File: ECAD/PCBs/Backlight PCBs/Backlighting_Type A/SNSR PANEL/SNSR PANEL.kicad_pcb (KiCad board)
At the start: 2 copper layers, 137.2 x 76.2 mm, 127 parts, among them J1 Conn_01x04_Female, J2 Conn_01x04_Female

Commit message: Drawing Sheet & Silkscreen update - Backlight Panels (Fc thru Spin)
1:  Updated/Relinked Drawing Sheet for both PCB and Schematics
2:  Standardized Silkscreen (if required)

Finished Remaining Backlighting Type A & Type B PCBs.....
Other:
- board text added: "SNSR PANEL Revision: 3 www.openhornet.com"
- board text removed: "SNSR Panel Backlight Designed by L. Walker"
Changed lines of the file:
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@@
   )
   (paper "A4")
+  (title_block
+    (title "SNSR PANEL")
+    (date "2023-02-10")
+    (rev "3")
+  )
   (layers
     (0 "F.Cu" signal)
@@
     (effects (font (size 1 1) (thickness 0.15)) (justify mirror))
   )
-  (gr_text "SNSR Panel Backlight\nDesigned by L. Walker" (at 121.2 83.4) (layer "B.SilkS")
-    (effects (font (size 1 1) (thickness 0.15)) (justify left mirror))
+  (gr_text "SNSR PANEL\nRevision: 3\nwww.openhornet.com" (at 156.4132 88.0618) (layer "B.SilkS")
+    (effects (font (size 1 1) (thickness 0.15)) (justify mirror))
   )
   (gr_text "POWER REQUIREMENTS:\nVOLTAGE: 5V DC\nLEDS: 58\nCURRENT: 3.48A\nWATTAGE: 17.4W" (at 199.7456 88.8746) (layer "B.SilkS")

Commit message: Review: SIM CTRL thru SPIN RCV 100% - minus SEL JETT
Reviewed/adjusted silkscreens as needed
Relinked footprints
Updated Manufacturing files
Updated PNGs and STEP files as needed.
Renamed PNGs for standardization
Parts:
- 1, 2: footprint OH_Backlighting:OH_Panel_6-32_PHS -> OH_Footprints:OH_Panel_6-32_PHS
- 3, 5: footprint OH_Backlighting:100SPX_Toggle_13mm_x_18mm -> OH_Footprints:100SPX_Toggle_13mm_x_18mm
- 4: footprint OH_Backlighting:631H_Toggle_13mm_x_13mm -> OH_Footprints:631H_Toggle_13mm_x_13mm
- G***: footprint OH_Backlighting:100SP3_Toggle_Silkscreen -> OH_Footprints:100SP3_Toggle_Silkscreen
- G***: footprint OH_Backlighting:631H_Toggle_Silkscreen -> OH_Footprints:631H_Toggle_Silkscreen
- G***: footprint OH_Backlighting:100SP1_Toggle_Silkscreen -> OH_Footprints:100SP1_Toggle_Silkscreen
- G***: footprint OH_General:CC-BY-NC-SA-Small -> OH_Footprints:CC-BY-NC-SA-Small
- G***: footprint OH_General:OH_LOGO_37.7mm_5.9mm -> OH_Footprints:OH_LOGO_37.7mm_5.9mm
- G*** (x2): footprint OH_Backlighting:A12505RNZQ - SWITCH, ROTARY, 45 DEG -> OH_Footprints:A12505RNZQ - SWITCH, ROTARY, 45 DEG

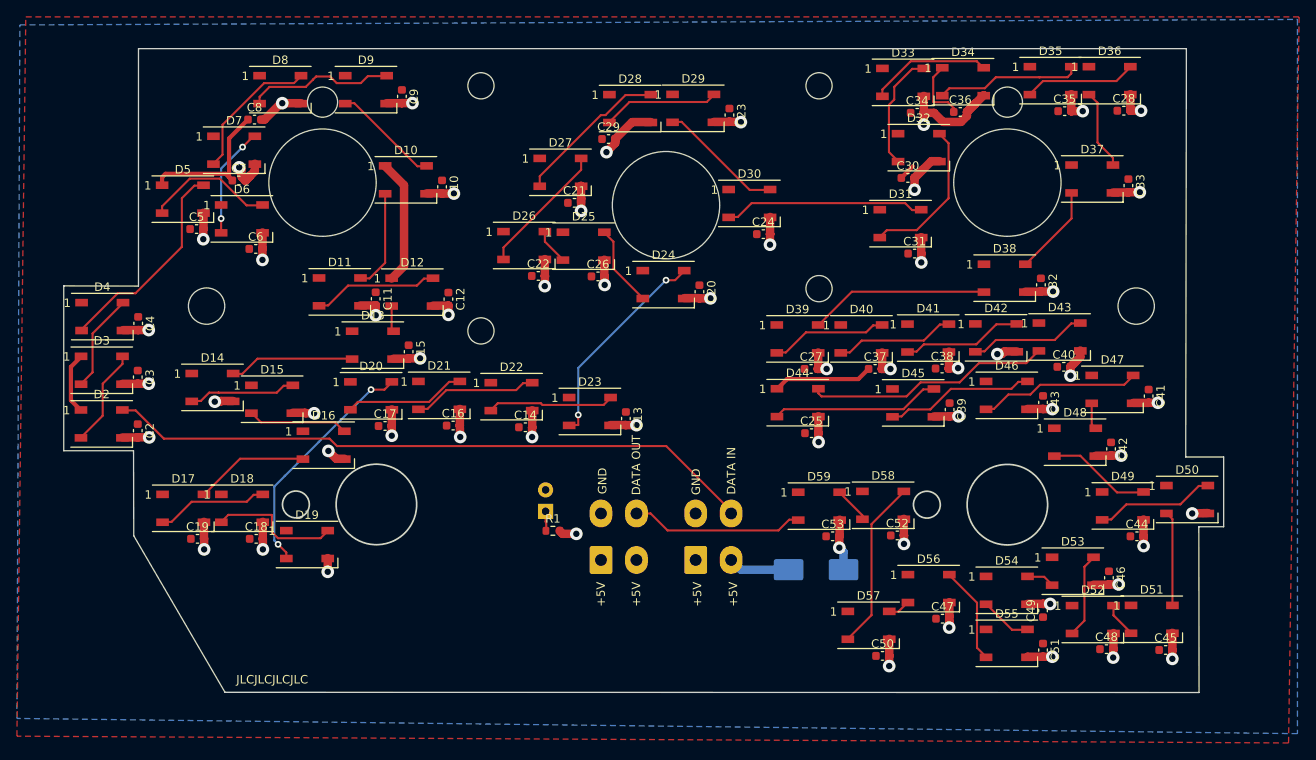
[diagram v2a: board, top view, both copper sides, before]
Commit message: KiCad 7 Transition - SNSR Panel
PCB and Schematic standardization
Updated silkscreen text
Adjusted traces to prevent conflicts
Add Testpoints
Recompiled assets and manufacturing files
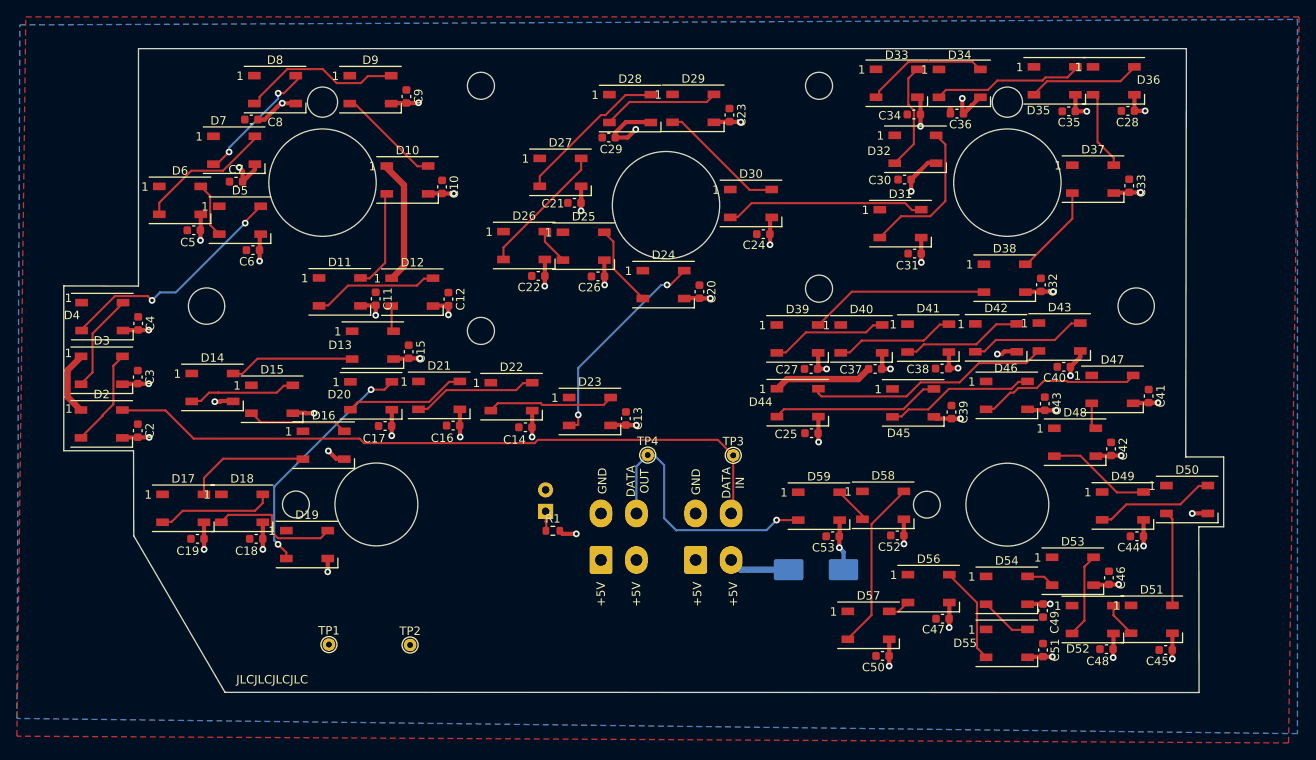
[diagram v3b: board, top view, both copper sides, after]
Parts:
- added MH10: Switch_Rotary_8pos45Deg, OH_Footprints:A12505RNZQ - SWITCH, ROTARY, 45 DEG, 8-POS, F.Cu at (117.6, 103.5)
- added MH11: Switch_Rotary_8pos45Deg, OH_Footprints:A12505RNZQ - SWITCH, ROTARY, 45 DEG, 8-POS, F.Cu at (192.3, 103.6)
- added MH3: M3 / 3.2mm, OH_Footprints:MountingHole_3.2mm_M3_DIN965, B.Cu at (130.0, 54.0)
- added MH4: M3 / 3.2mm, OH_Footprints:MountingHole_3.2mm_M3_DIN965, B.Cu at (170.0, 54.0)
- added MH5: M3 / 3.2mm, OH_Footprints:MountingHole_3.2mm_M3_DIN965, B.Cu at (130.0, 83.0)
- added MH6: M3 / 3.2mm, OH_Footprints:MountingHole_3.2mm_M3_DIN965, B.Cu at (170.0, 78.0)
- added TP1: TestPoint, OH_Footprints:TestPoint_THTPad_D1.5mm_Drill0.7mm, F.Cu at (112.0, 120.1)
- added TP2: TestPoint, OH_Footprints:TestPoint_THTPad_D1.5mm_Drill0.7mm, F.Cu at (121.6, 120.2)
- added TP3: TestPoint, OH_Footprints:TestPoint_THTPad_D1.5mm_Drill0.7mm, F.Cu at (159.8, 97.7)
- added TP4: TestPoint, OH_Footprints:TestPoint_THTPad_D1.5mm_Drill0.7mm, F.Cu at (149.7, 97.7)
- C1: value C_Polarized -> 1000uF
- C10, C11, C12, C13, C14, C15, C16, C17, C18, C19, C2, C20, C21, C22, C23, C24, C25, C26, C27, C28, C29, C3, C30, C31, C32, C33, C34, C35, C36, C37, C38, C39, C4, C40, C41, C42, C43, C44, C45, C46, C47, C48, C49, C5, C50, C51, C52, C53, C6, C7, C8, C9: value C -> 0.1uF
- D1: value LED -> Green
- J1, J2: value Conn_01x04_Female -> Mini-Fit Jr. 2x02
- LOGO1: renamed from G***; footprint OH_Footprints:OH_LOGO_37.7mm_5.9mm -> OH_Footprints:LOGO_OH_Text_Small
- LOGO2: renamed from G***; footprint OH_Footprints:CC-BY-NC-SA-Small -> OH_Footprints:LOGO_CC-BY-NC-SA_Half_Small
- LOGO3: renamed from G***; value 100SP3 Toggle -> LOGO; moved to B.Cu
- LOGO4: renamed from G***; value 631H Toggle -> LOGO; footprint OH_Footprints:631H_Toggle_Silkscreen -> OH_Footprints:631H2_Toggle_Silkscreen; moved to B.Cu
- LOGO5: renamed from G***; value 100SP1 Toggle -> LOGO; moved to B.Cu
- MH1: renamed from 2; value OH_Panel_Fastner_Keepout -> 6x32 / 4mm; footprint OH_Footprints:OH_Panel_6-32_PHS -> OH_Footprints:MountingHole_6-32_PHS; moved to B.Cu
- MH2: renamed from 1; value OH_Panel_Fastner_Keepout -> 6x32 / 4mm; footprint OH_Footprints:OH_Panel_6-32_PHS -> OH_Footprints:MountingHole_6-32_PHS; moved to B.Cu
- MH7: renamed from 3; value 100SPX_Toggle_13mm_x_18mm -> Switch_100SPx
- MH8: renamed from 5; value 100SPX_Toggle_13mm_x_18mm -> Switch_100SPx
- MH9: renamed from 4; value 631H_Toggle_13mm_x_13mm -> Switch_631H; footprint OH_Footprints:631H_Toggle_13mm_x_13mm -> OH_Footprints:631HX_Toggle_13mm_x_13mm
- R1: value R -> 470
- moved LOGO2 83.5 mm to (160.5, 50.1)
- moved LOGO1 2.08 mm to (153.6, 122.2)
- moved LOGO5 1.36 mm to (202.7, 64.9), turned to 180 degrees
- moved LOGO4 0.77 mm to (163.4, 67.0), turned to 180 degrees
- moved D33 0.76 mm to (179.2, 53.7)
- moved LOGO3 0.70 mm to (121.8, 65.0), turned to 180 degrees
- moved D8 0.62 mm to (105.6, 54.5)
- moved C9 0.53 mm to (121.2, 55.3)
- moved D9 0.53 mm to (116.9, 54.5)
- moved D35 0.48 mm to (197.9, 53.4)
- moved D36 0.48 mm to (204.9, 53.4)
- moved C28 0.48 mm to (206.5, 57.0)
- moved C35 0.48 mm to (199.5, 57.0)
- moved C34 0.44 mm to (181.2, 57.4)
- moved D32 0.44 mm to (181.4, 61.5)
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- renumbered D6 to D5, D5 to D6, G*** to LOGO6, G*** to LOGO7
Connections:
- net /DATAIN renamed DATA IN
- net /DATAOUT renamed DATA OUT
- net /LED+5V renamed +5V
- net /LEDGND renamed GND
- net Net-(D16-Pad2) renamed /DATA1
- net Net-(D31-Pad2) renamed /DATA2
- net Net-(D45-Pad2) renamed /DATA3
- D4 pad 2: Net-(D4-Pad2) -> Net-(D4-DOUT)
- D5 pad 2: Net-(D6-Pad2) -> Net-(D5-DOUT)
- D5 pad 4: Net-(D5-Pad2) -> Net-(D4-DOUT)
- D6 pad 2: Net-(D5-Pad2) -> Net-(D6-DOUT)
- D6 pad 4: Net-(D4-Pad2) -> Net-(D5-DOUT)
- D7 pad 4: Net-(D6-Pad2) -> Net-(D6-DOUT)
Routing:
- net Net-(D4-DOUT): track 0.00 -> 27.7 mm, vias 0 -> 2
- net +5V: track 68.9 -> 42.0 mm
- net Net-(D4-Pad2): track 24.9 -> 0.00 mm
- net Net-(D6-DOUT): track 0.00 -> 15.8 mm
- net Net-(D5-Pad2): track 15.3 -> 0.00 mm
- net Net-(D6-Pad2): track 13.1 -> 0.00 mm, vias 2 -> 0
- net DATA OUT: track 20.5 -> 33.1 mm, vias 0 -> 1
- net Net-(D5-DOUT): track 0.00 -> 6.56 mm
- net GND: track 202.6 -> 196.8 mm, vias 58 -> 59
- net DATA IN: track 77.2 -> 81.4 mm
- net Net-(D7-DOUT): track 16.7 -> 14.9 mm, vias 0 -> 2
- net /DATA1: track 13.5 -> 14.6 mm
- net Net-(D32-DOUT): track 13.9 -> 12.8 mm
- net Net-(D10-DIN): track 12.7 -> 11.6 mm
- net Net-(D8-DOUT): track 17.5 -> 18.2 mm
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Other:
- outline, holes or cut-outs redrawn
- board text added: "0.2000 mm / 0.0000 mm"
- board text added: "0.3000 mm"
- board text added: "1.6000 mm"
- board text added: "137.2300 mm x 76.1762 mm"
- board text added: "BOARD CHARACTERISTICS"
- board text added: "Board Thickness:"
- board text added: "Board overall dimensions:"
- board text added: "Castellated pads:"
- board text added: "Copper Finish:"
- board text added: "Copper Layer Count:"
- board text added: "Edge card connectors:"
- board text added: "Impedance Control:"
- board text added: "Min hole diameter:"
- board text added: "Min track/spacing:"
- board text added: "No"
- board text added: "None"
- board text added: "Plated Board Edge:"
- board text added: "SNSR PANEL REV: 4 WWW.OPENHORNET.COM"
- board text removed: "IN"
- board text removed: "SNSR PANEL Revision: 3 www.openhornet.com"
- board text removed: "Switch PCB H1"
- board text removed: "Switch PCB H2"
- board text removed: "Switch PCB H3"
- board text removed: "Switch PCB H4"
- board text removed: "THRU"
- board text removed: "⌀3MM"
